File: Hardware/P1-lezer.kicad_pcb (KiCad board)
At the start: 2 copper layers, 70 x 30 mm, 13 parts, among them J1 RJ12, M2.5 MountingHole_2.7mm_M2.5_ISO73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, Q1 BC547, U1 WeMos_D1_mini, U2 TIL111

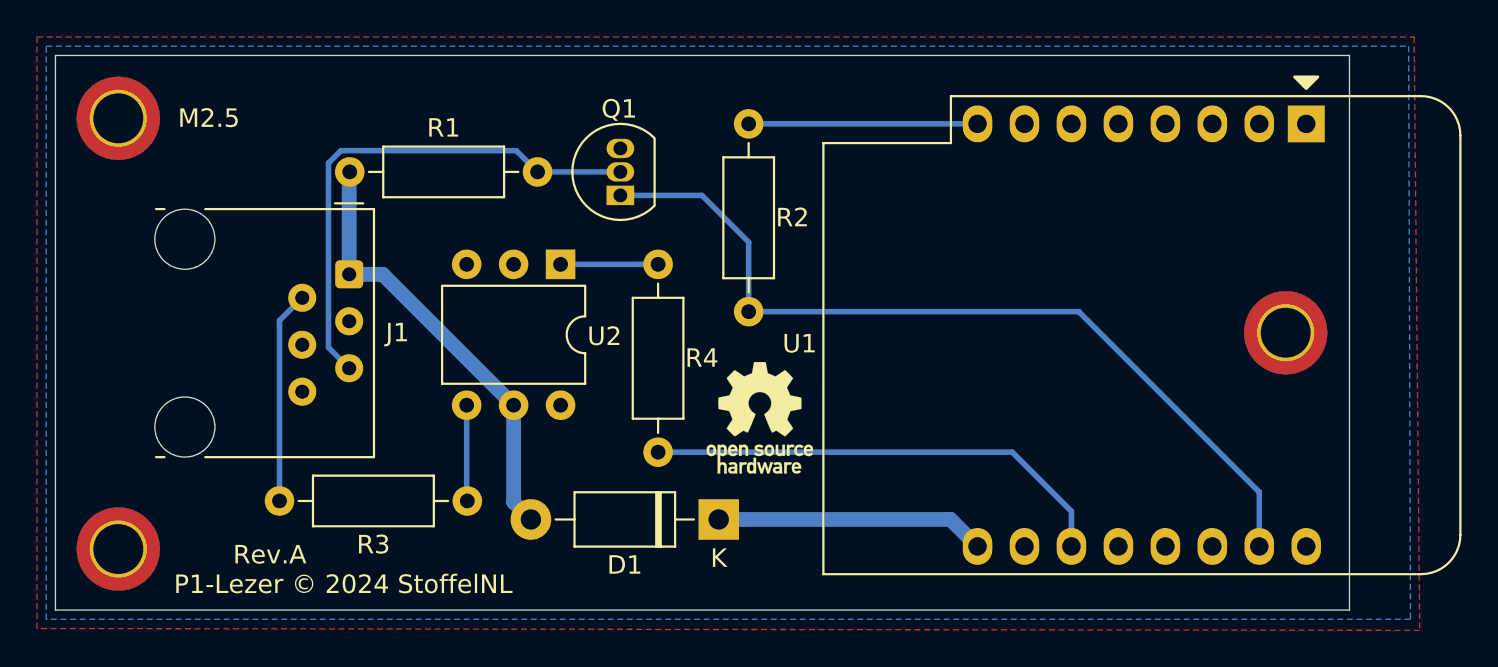
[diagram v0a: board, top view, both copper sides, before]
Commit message: re-routed signal slightly, checked RJ12 dimensions, regenerated gerbers.
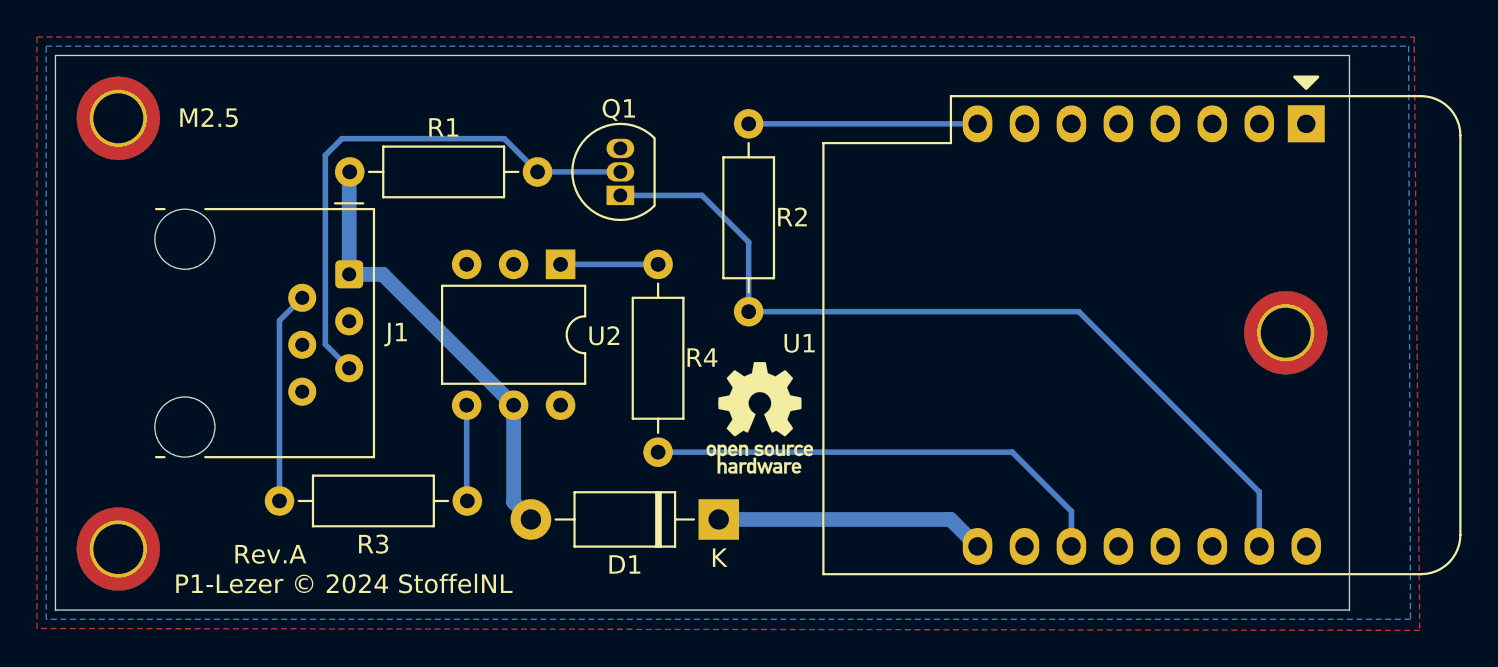
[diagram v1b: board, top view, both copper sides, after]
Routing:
- net Net-(Q1-B): track 28.1 -> 29.1 mm
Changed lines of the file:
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@@
 				(font
 					(size 1 1)
-					(thickness 0.15)
+					(thickness 0.153)
 				)
 			)
@@
 				(font
 					(size 1 1)
-					(thickness 0.15)
+					(thickness 0.153)
 				)
 			)
@@
 				(font
 					(size 1 1)
-					(thickness 0.15)
+					(thickness 0.153)
 				)
 			)
@@
 				(font
 					(size 1 1)
-					(thickness 0.15)
+					(thickness 0.153)
 				)
 			)
@@
 				(font
 					(size 1 1)
-					(thickness 0.15)
+					(thickness 0.153)
 				)
 			)
@@
 				(font
 					(size 1 1)
-					(thickness 0.15)
+					(thickness 0.153)
 				)
 			)
@@
 				(font
 					(size 1 1)
-					(thickness 0.15)
+					(thickness 0.153)
 				)
 			)
@@
 				(font
 					(size 1 1)
-					(thickness 0.15)
+					(thickness 0.153)
 				)
 			)
@@
 	)
 	(segment
-		(start 80.37 72.823654)
-		(end 81.043654 72.15)
+		(start 91.68 73.3)
+		(end 96.16 73.3)
 		(width 0.3)
 		(layer "B.Cu")
@@
 	)
 	(segment
-		(start 91.68 73.3)
-		(end 96.16 73.3)
+		(start 80.2 82.63)
+		(end 80.2 72.4)
 		(width 0.3)
 		(layer "B.Cu")
@@
 	)
 	(segment
-		(start 80.37 82.8)
-		(end 80.37 72.823654)
+		(start 81.49 83.92)
+		(end 80.2 82.63)
 		(width 0.3)
 		(layer "B.Cu")
@@
 	)
 	(segment
-		(start 90.53 72.15)
-		(end 91.68 73.3)
+		(start 81.1 71.5)
+		(end 89.88 71.5)
 		(width 0.3)
 		(layer "B.Cu")
@@
 	)
 	(segment
-		(start 81.49 83.92)
-		(end 80.37 82.8)
+		(start 80.2 72.4)
+		(end 81.1 71.5)
 		(width 0.3)
 		(layer "B.Cu")
@@
 	)
 	(segment
-		(start 81.043654 72.15)
-		(end 90.53 72.15)
+		(start 89.88 71.5)
+		(end 91.68 73.3)
 		(width 0.3)
 		(layer "B.Cu")
